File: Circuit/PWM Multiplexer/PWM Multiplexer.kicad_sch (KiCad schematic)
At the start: 3 parts

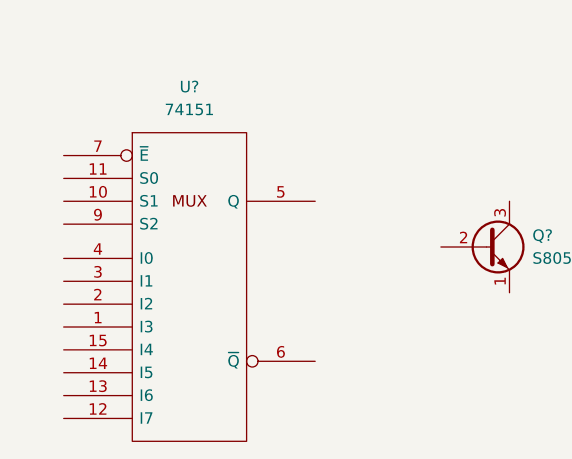
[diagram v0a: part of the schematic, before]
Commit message: Modified unipolar driver code and PWM multiplexer circuit
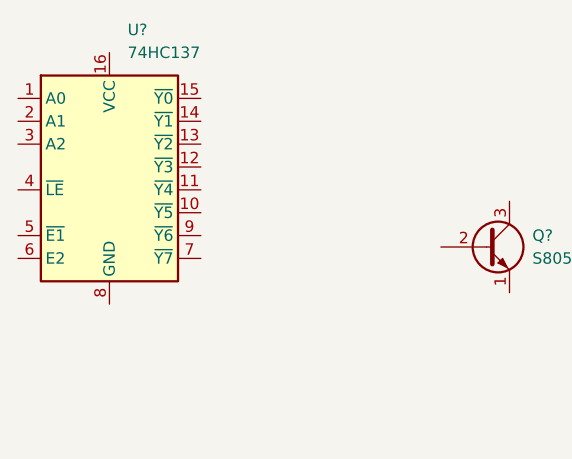
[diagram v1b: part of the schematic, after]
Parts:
- removed U?: 74151, symbol 74xx_IEEE:74151
- added U?: 74HC137, symbol 74xx:74HC137
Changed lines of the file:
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@@
 (kicad_sch (version 20211123) (generator eeschema)
   (paper "A4")
+  (symbol (lib_id "74xx:74HC137") (at 106.68 85.09 0) (unit 1)
+    (in_bom yes) (on_board yes) (fields_autoplaced)
+    (property "Reference" "U?" (id 0) (at 108.6994 67.31 0)
+      (effects (font (size 1.27 1.27)) (justify left))
+    )
+    (property "Value" "74HC137" (id 1) (at 108.6994 69.85 0)
+      (effects (font (size 1.27 1.27)) (justify left))
+    )
+    (property "Footprint" "" (id 2) (at 106.68 85.09 0)
+      (effects (font (size 1.27 1.27)) hide)
+    )
+    (property "Datasheet" "http://www.ti.com/lit/ds/symlink/cd74hc237.pdf" (id 3) (at 106.68 85.09 0)
+      (effects (font (size 1.27 1.27)) hide)
+    )
+    (pin "1")
+    (pin "10")
+    (pin "11")
+    (pin "12")
+    (pin "13")
+    (pin "14")
+    (pin "15")
+    (pin "16")
+    (pin "2")
+    (pin "3")
+    (pin "4")
+    (pin "5")
+    (pin "6")
+    (pin "7")
+    (pin "8")
+    (pin "9")
+  )
   (symbol (lib_id "Transistor_BJT:S8050") (at 148.59 91.44 0) (unit 1)
     (in_bom yes) (on_board yes) (fields_autoplaced)
@@
     (pin "3")
   )
-  (symbol (lib_id "74xx_IEEE:74151") (at 115.57 95.25 0) (unit 1)
-    (in_bom yes) (on_board yes) (fields_autoplaced)
-    (property "Reference" "U?" (id 0) (at 115.57 73.66 0))
-    (property "Value" "74151" (id 1) (at 115.57 76.2 0))
-    (property "Footprint" "" (id 2) (at 115.57 95.25 0)
-      (effects (font (size 1.27 1.27)) hide)
-    )
-    (property "Datasheet" "" (id 3) (at 115.57 95.25 0)
-      (effects (font (size 1.27 1.27)) hide)
-    )
-    (pin "16")
-    (pin "8")
-    (pin "1")
-    (pin "10")
-    (pin "11")
-    (pin "12")
-    (pin "13")
-    (pin "14")
-    (pin "15")
-    (pin "2")
-    (pin "3")
-    (pin "4")
-    (pin "5")
-    (pin "6")
-    (pin "7")
-    (pin "9")
-  )
   (sheet_instances
     (path "/" (page "1"))
@@
       (reference "Q?") (unit 1) (value "S8050") (footprint "Package_TO_SOT_THT:TO-92_Inline")
     )
-    (path "/eebbaa6e-a7b3-4601-834f-b7edd8c79450"
-      (reference "U?") (unit 1) (value "74151") (footprint "")
+    (path "/052d86b5-bde2-4468-bc83-6d4af3b11aa7"
+      (reference "U?") (unit 1) (value "74HC137") (footprint "")
     )
   )

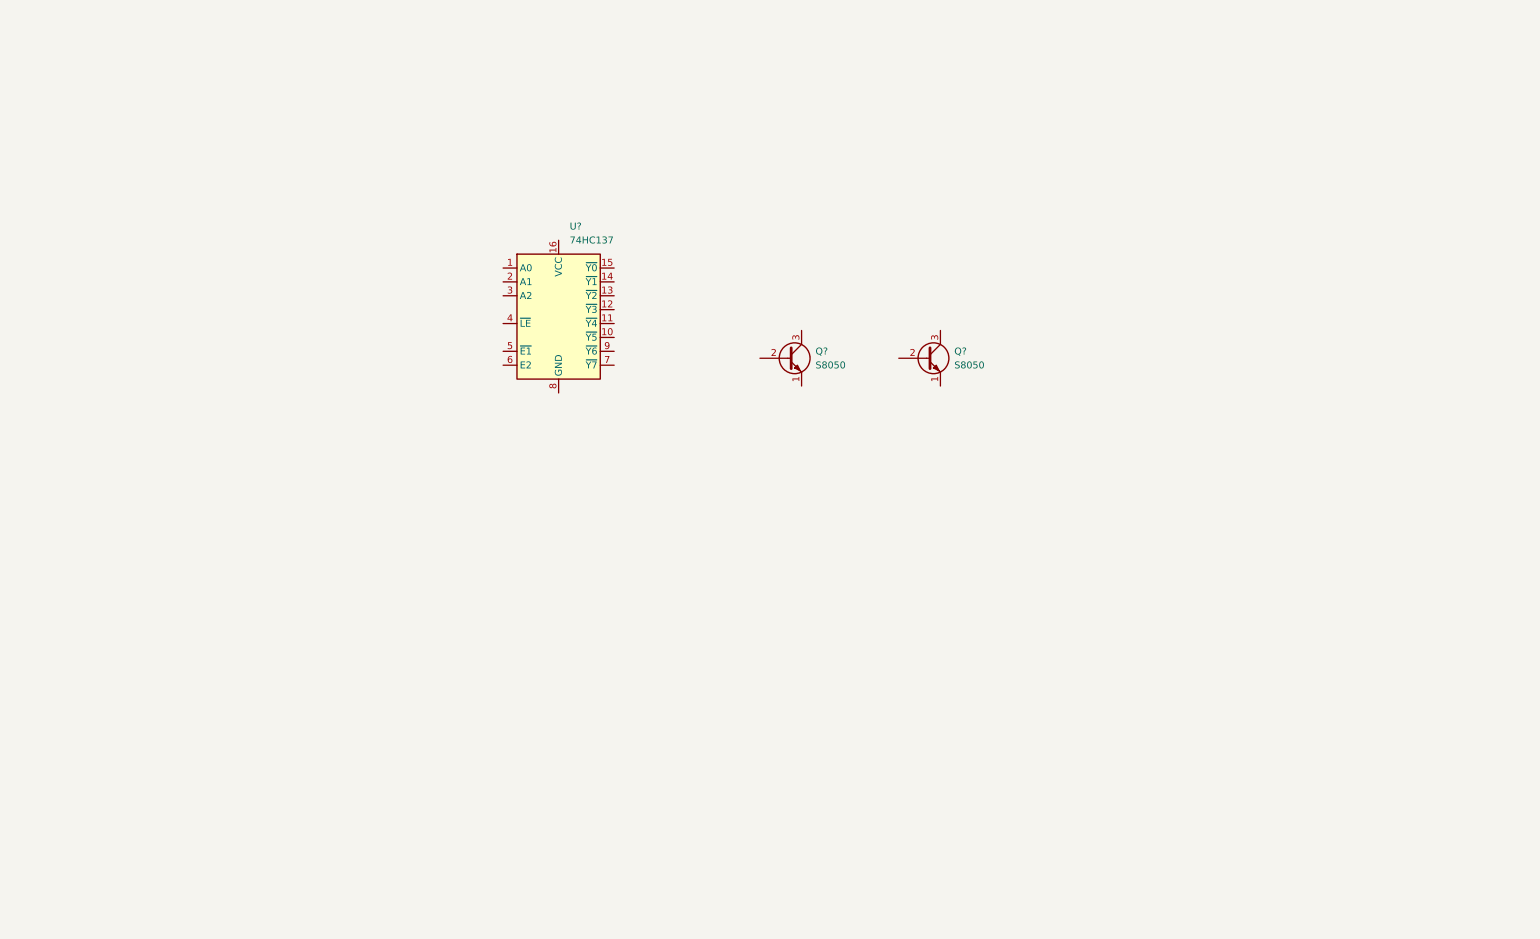
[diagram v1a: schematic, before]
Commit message: Finished PWM Multiplexer circuit schematics and started PCB design
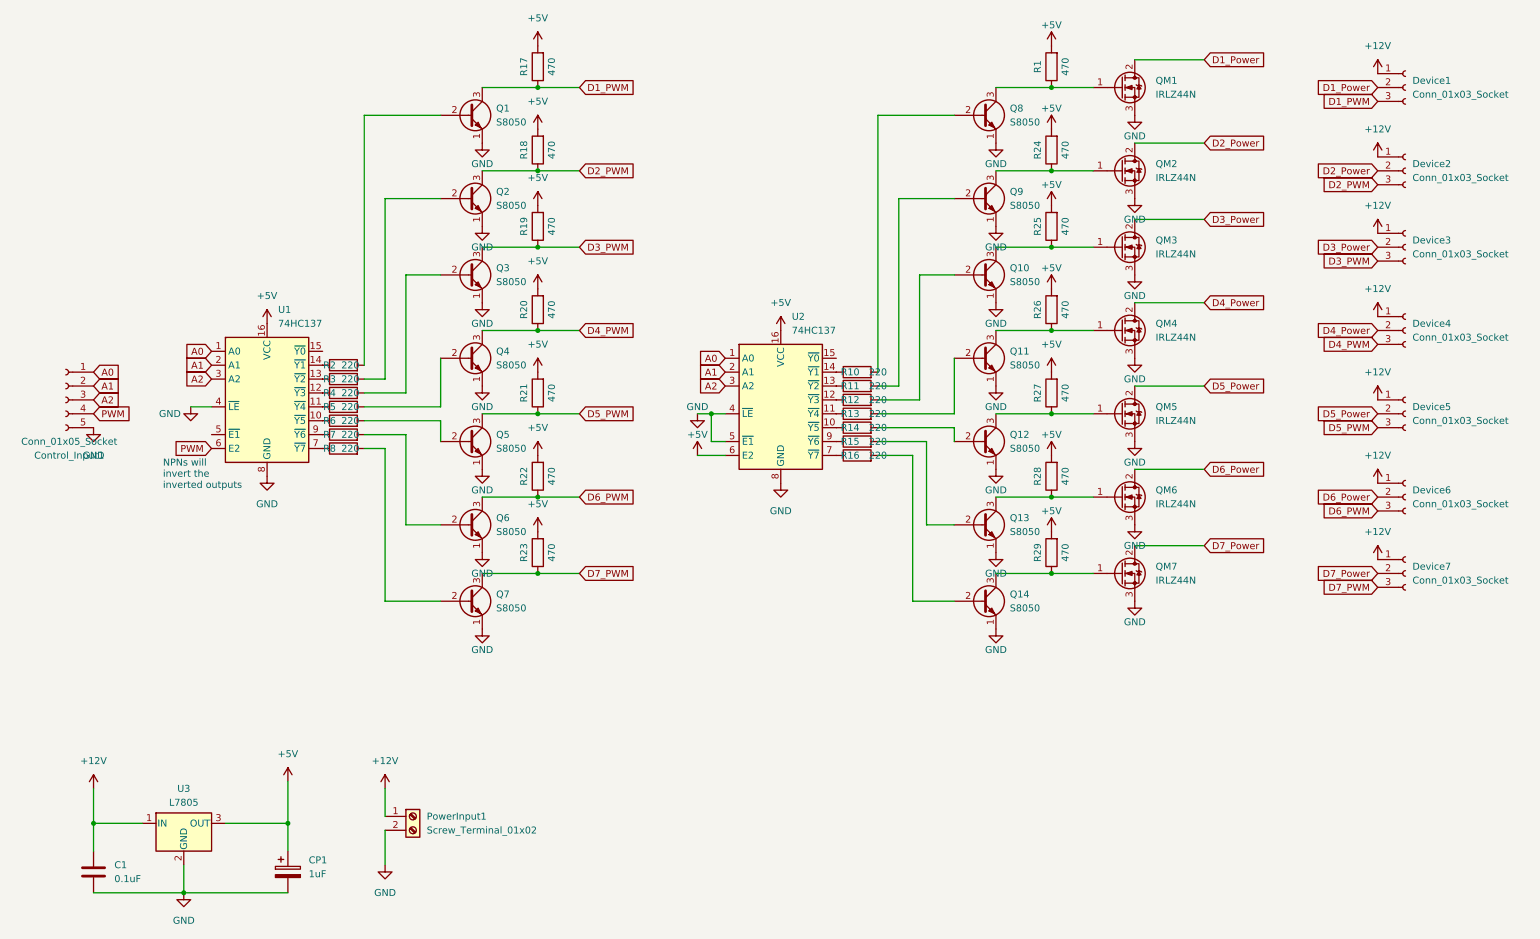
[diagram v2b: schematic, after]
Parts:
- removed Q? (x2): S8050, Package_TO_SOT_THT:TO-92_Inline, symbol Transistor_BJT:S8050
- added C1: 0.1uF, Capacitor_THT:C_Disc_D5.0mm_W2.5mm_P2.50mm, symbol Device:C
- added CP1: 1uF, Capacitor_THT:CP_Radial_D5.0mm_P2.50mm, symbol Device:C_Polarized
- added Control_Input1: Conn_01x05_Socket, Connector_PinSocket_2.54mm:PinSocket_1x05_P2.54mm_Horizontal, symbol Connector:Conn_01x05_Socket
- added Device1, Device2, Device3, Device4, Device5, Device6, Device7: Conn_01x03_Socket, Connector_PinSocket_2.54mm:PinSocket_1x03_P2.54mm_Horizontal, symbol Connector:Conn_01x03_Socket
- added PowerInput1: Screw_Terminal_01x02, TerminalBlock:TerminalBlock_bornier-2_P5.08mm, symbol Connector:Screw_Terminal_01x02
- added Q1, Q10, Q11, Q12, Q13, Q14, Q2, Q3, Q4, Q5, Q6, Q7, Q8, Q9: S8050, Package_TO_SOT_THT:TO-92_Inline, symbol Transistor_BJT:S8050
- added QM1, QM2, QM3, QM4, QM5, QM6, QM7: IRLZ44N, Package_TO_SOT_THT:TO-220-3_Vertical, symbol Transistor_FET:IRLZ44N
- added R1, R17, R18, R19, R20, R21, R22, R23, R24, R25, R26, R27, R28, R29: 470, Resistor_THT:R_Axial_DIN0207_L6.3mm_D2.5mm_P7.62mm_Horizontal, symbol Device:R
- added R10, R11, R12, R13, R14, R15, R16, R2, R3, R4, R5, R6, R7, R8: 220, Resistor_THT:R_Axial_DIN0207_L6.3mm_D2.5mm_P7.62mm_Horizontal, symbol Device:R
- added U2: 74HC137, Package_DIP:DIP-16_W7.62mm_Socket_LongPads, symbol 74xx:74HC137
- added U3: L7805, Package_TO_SOT_THT:TO-220-3_Vertical, symbol Regulator_Linear:L7805
- U1: renamed from U?; footprint (none) -> Package_DIP:DIP-16_W7.62mm_Socket_LongPads
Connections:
- net A0: now reaches U1.1 (A0)
- net A0: now also Control_Input1.1 (Pin_1), U2.1 (A0)
- net at U1.10 (~{Y5}): now also R6.1
- net at U1.11 (~{Y4}): now also R5.1
- net at U1.12 (~{Y3}): now also R4.1
- net at U1.13 (~{Y2}): now also R3.1
- net at U1.14 (~{Y1}): now also R2.1
- net +5V: now reaches U1.16 (VCC)
- net +5V: now also CP1.1, R1.2, R17.2, R18.2, R19.2, R20.2, R21.2, R22.2, R23.2, R24.2, R25.2, R26.2, R27.2, R28.2, R29.2, U2.16 (VCC), U2.6 (E2), U3.3 (OUT)
- net A1: now reaches U1.2 (A1)
- net A1: now also Control_Input1.2 (Pin_2), U2.2 (A1)
- net A2: now reaches U1.3 (A2)
- net A2: now also Control_Input1.3 (Pin_3), U2.3 (A2)
- net GND: now reaches U1.4 (~{LE})
- net GND: now also U1.8 (GND), C1.2, CP1.2, Control_Input1.5 (Pin_5), PowerInput1.2 (Pin_2), Q1.1 (E), Q10.1 (E), Q11.1 (E), Q12.1 (E), Q13.1 (E), Q14.1 (E), Q2.1 (E), Q3.1 (E), Q4.1 (E), Q5.1 (E), Q6.1 (E), Q7.1 (E), Q8.1 (E), Q9.1 (E), QM1.3 (S), QM2.3 (S), QM3.3 (S), QM4.3 (S), QM5.3 (S), QM6.3 (S), QM7.3 (S), U2.4 (~{LE}), U2.5 (~{E1}), U2.8 (GND), U3.2 (GND)
- net PWM: now reaches U1.6 (E2)
- net PWM: now also Control_Input1.4 (Pin_4)
- net at U1.7 (~{Y7}): now also R8.1
- net at U1.9 (~{Y6}): now also R7.1
- new net: Q6.2 (B), R7.2
- new net: Q11.3 (C), QM4.1 (G), R26.1
- new net: Q3.2 (B), R4.2
- new net: Q7.2 (B), R8.2
- new net: Q12.3 (C), QM5.1 (G), R27.1
- new net: Q14.2 (B), R16.2
- new net: Q14.3 (C), QM7.1 (G), R29.1
- new net: Q8.3 (C), QM1.1 (G), R1.1
- new net: Q11.2 (B), R13.2
- new net: Q2.2 (B), R3.2
- new net: R14.1, U2.10 (~{Y5})
- new net: Q12.2 (B), R14.2
- new net: Q9.3 (C), QM2.1 (G), R24.1
- new net: Q13.3 (C), QM6.1 (G), R28.1
- new net: R10.1, U2.14 (~{Y1})
- new net: Q8.2 (B), R10.2
- new net: R16.1, U2.7 (~{Y7})
- new net: Q10.3 (C), QM3.1 (G), R25.1
- new net: R13.1, U2.11 (~{Y4})
- new net: Q4.2 (B), R5.2
- new net: R12.1, U2.12 (~{Y3})
- new net: Q10.2 (B), R12.2
- new net: R11.1, U2.13 (~{Y2})
- new net: R15.1, U2.9 (~{Y6})
- new net: Q1.2 (B), R2.2
- new net: Q5.2 (B), R6.2
- new net: Q9.2 (B), R11.2
- new net: Q13.2 (B), R15.2
- new net +12V: C1.1, Device1.1 (Pin_1), Device2.1 (Pin_1), Device3.1 (Pin_1), Device4.1 (Pin_1), Device5.1 (Pin_1), Device6.1 (Pin_1), Device7.1 (Pin_1), PowerInput1.1 (Pin_1), U3.1 (IN)
- new net D1_PWM: Device1.3 (Pin_3), Q1.3 (C), R17.1
- new net D1_Power: Device1.2 (Pin_2), QM1.2 (D)
- new net D2_PWM: Device2.3 (Pin_3), Q2.3 (C), R18.1
- new net D2_Power: Device2.2 (Pin_2), QM2.2 (D)
- new net D3_PWM: Device3.3 (Pin_3), Q3.3 (C), R19.1
- new net D3_Power: Device3.2 (Pin_2), QM3.2 (D)
- new net D4_PWM: Device4.3 (Pin_3), Q4.3 (C), R20.1
- new net D4_Power: Device4.2 (Pin_2), QM4.2 (D)
- new net D5_PWM: Device5.3 (Pin_3), Q5.3 (C), R21.1
- new net D5_Power: Device5.2 (Pin_2), QM5.2 (D)
- new net D6_PWM: Device6.3 (Pin_3), Q6.3 (C), R22.1
- new net D6_Power: Device6.2 (Pin_2), QM6.2 (D)
- new net D7_PWM: Device7.3 (Pin_3), Q7.3 (C), R23.1
- new net D7_Power: Device7.2 (Pin_2), QM7.2 (D)
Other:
- note added: "NPNs will invert the inverted outputs"
- moved on the sheet: U1

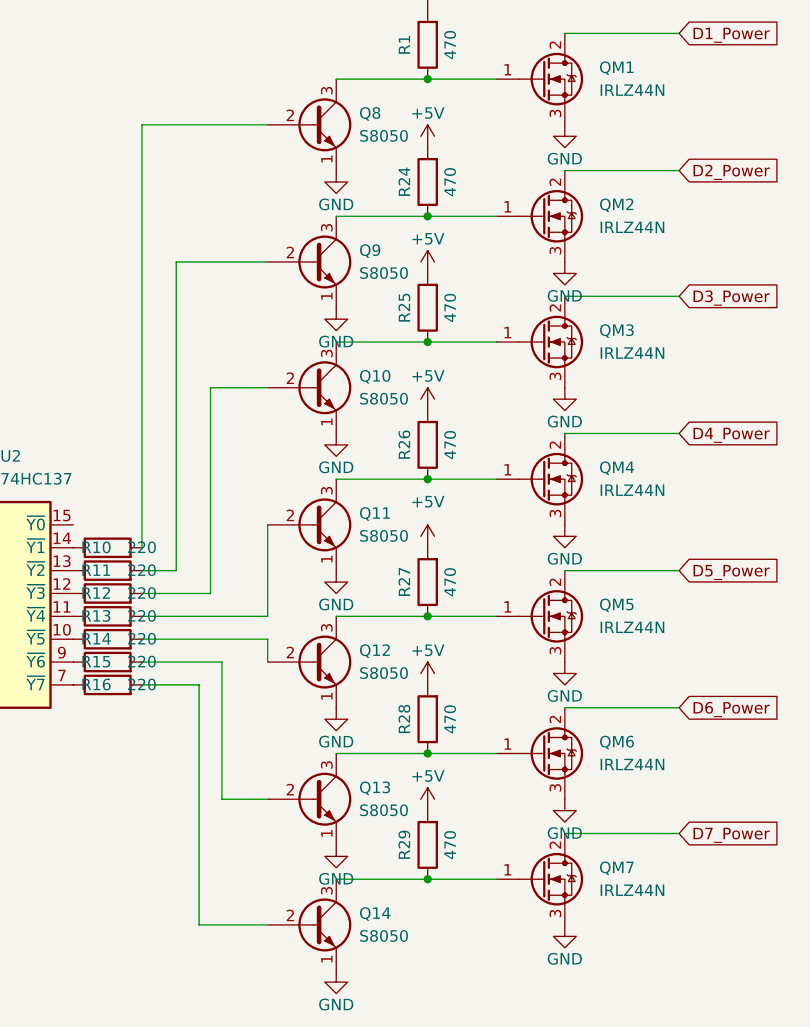
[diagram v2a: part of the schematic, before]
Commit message: PWM multiplexer circuit PCB traces ALL connected in a preliminary manner
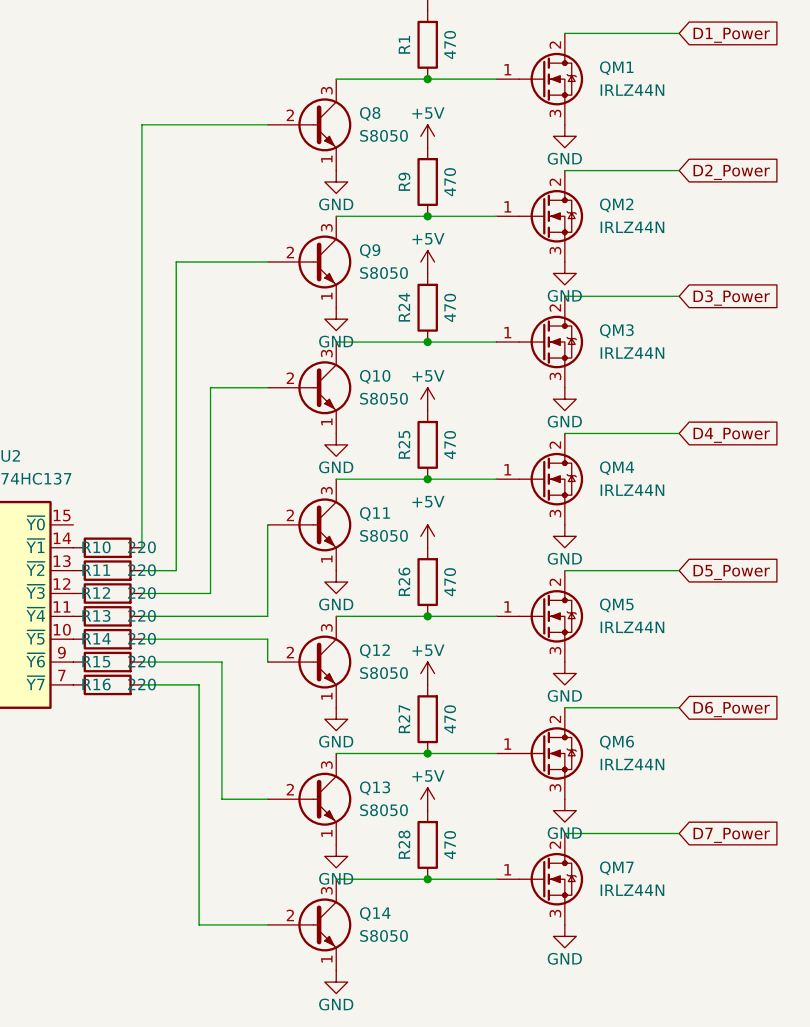
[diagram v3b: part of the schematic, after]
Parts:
- removed R29: 470, Resistor_THT:R_Axial_DIN0207_L6.3mm_D2.5mm_P7.62mm_Horizontal, symbol Device:R
- added R9: 470, Resistor_THT:R_Axial_DIN0207_L6.3mm_D2.5mm_P10.16mm_Horizontal, symbol Device:R
- R1, R17, R18, R19, R20, R21, R22, R23, R24, R25, R26, R27, R28: footprint Resistor_THT:R_Axial_DIN0207_L6.3mm_D2.5mm_P7.62mm_Horizontal -> Resistor_THT:R_Axial_DIN0207_L6.3mm_D2.5mm_P10.16mm_Horizontal
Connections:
- net +5V: now also R9.2
- net at Q11.3 (C), QM4.1 (G): now also R25.1; no longer R26.1
- net at Q12.3 (C), QM5.1 (G): now also R26.1; no longer R27.1
- net at Q14.3 (C), QM7.1 (G): now also R28.1
- net at Q9.3 (C), QM2.1 (G): now also R9.1; no longer R24.1
- net at Q13.3 (C), QM6.1 (G): now also R27.1; no longer R28.1
- net at Q10.3 (C), QM3.1 (G): now also R24.1; no longer R25.1
